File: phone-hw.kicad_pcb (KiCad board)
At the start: 2 copper layers, 66 x 100 mm, 73 parts, among them J1 USB_C_Receptacle_USB2.0, J2 Conn_01x06, J4 SIM_Card, J5 BATT+, J6 BATT-, Q1 BC847BLT3G, Q2 S9015, Q3 RU8205G, SW1 SW_Push, SW2 SW_Push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

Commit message: route pcb
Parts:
- added R20: 10k, Resistor_SMD:R_0603_1608Metric_Pad1.05x0.95mm_HandSolder, F.Cu at (41.8, 89.2)
- J2: value Conn_01x06 -> Micro_SD_Card; footprint Connector:Tag-Connect_TC2030-IDC-NL_2x03_P1.27mm_Vertical -> Connector_Card:microSD_HC_Hirose_DM3D-SF; moved to B.Cu
- moved J2 62.0 mm to (29.5, 99.0), turned to 180 degrees
- moved R6 28.8 mm to (31.2, 84.8), turned to 180 degrees
- moved C4 0.56 mm to (29.8, 56.0)
- moved R8 0.50 mm to (26.5, 86.8)
- moved C15 0.25 mm to (53.8, 108.0)
- moved R7 0.25 mm to (30.5, 86.8)
- moved C24 0.13 mm to (74.5, 91.9), turned to 0 degrees
- turned R18 to 270 degrees
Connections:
- net JTAG_MTDI renamed SD_~CS
- J2 pad 1: VDD -> Net-(J2-Pad1)
- J2 pad 3: JTAG_MTCK -> SD_MOSI
- J2 pad 4: JTAG_MTMS -> VDD
- J2 pad 5: JTAG_MTDO -> SD_CLK
- U1 pad 13: JTAG_MTMS -> SD_CLK
- U1 pad 16: JTAG_MTCK -> SD_MISO
- U1 pad 23: JTAG_MTDO -> SD_MOSI
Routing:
- net GND_OUT: track 0.00 -> 274.1 mm, vias 0 -> 28
- net +BATT: track 0.00 -> 256.0 mm, vias 0 -> 10
- net VDD: track 0.00 -> 254.5 mm, vias 0 -> 22
- net LCD_TE: track 0.00 -> 115.5 mm, vias 0 -> 4
- net Net-(R1-Pad2): track 0.00 -> 114.4 mm, vias 0 -> 6
- net LCD_DC: track 0.00 -> 111.0 mm, vias 0 -> 2
- net LCD_SCL: track 0.00 -> 109.2 mm, vias 0 -> 2
- net LCD_SDA: track 0.00 -> 108.7 mm, vias 0 -> 2
- net LCD_~CS: track 0.00 -> 104.0 mm
- net GPS_RXD: track 0.00 -> 91.4 mm, vias 0 -> 2
- net BATT_~STDBY: track 0.00 -> 90.6 mm, vias 0 -> 6
- net Net-(SW2-Pad1): track 0.00 -> 88.8 mm, vias 0 -> 6
- net GPS_RESET: track 0.00 -> 87.6 mm, vias 0 -> 2
- net BATT_~CHRG: track 0.00 -> 87.6 mm
- net GPS_TXD: track 0.00 -> 81.8 mm, vias 0 -> 2
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- added copper zone on B.Cu, net GND_OUT

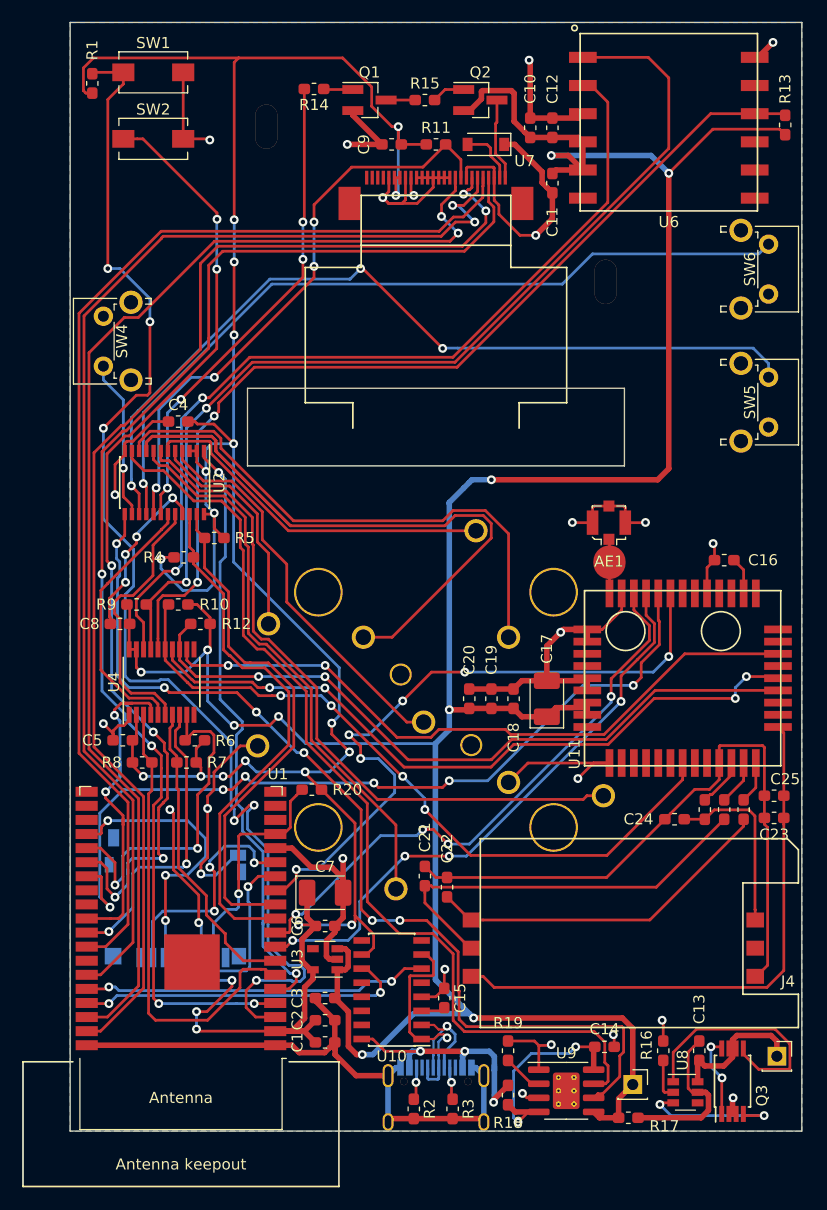
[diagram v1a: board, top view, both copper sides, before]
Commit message: add mounting holes
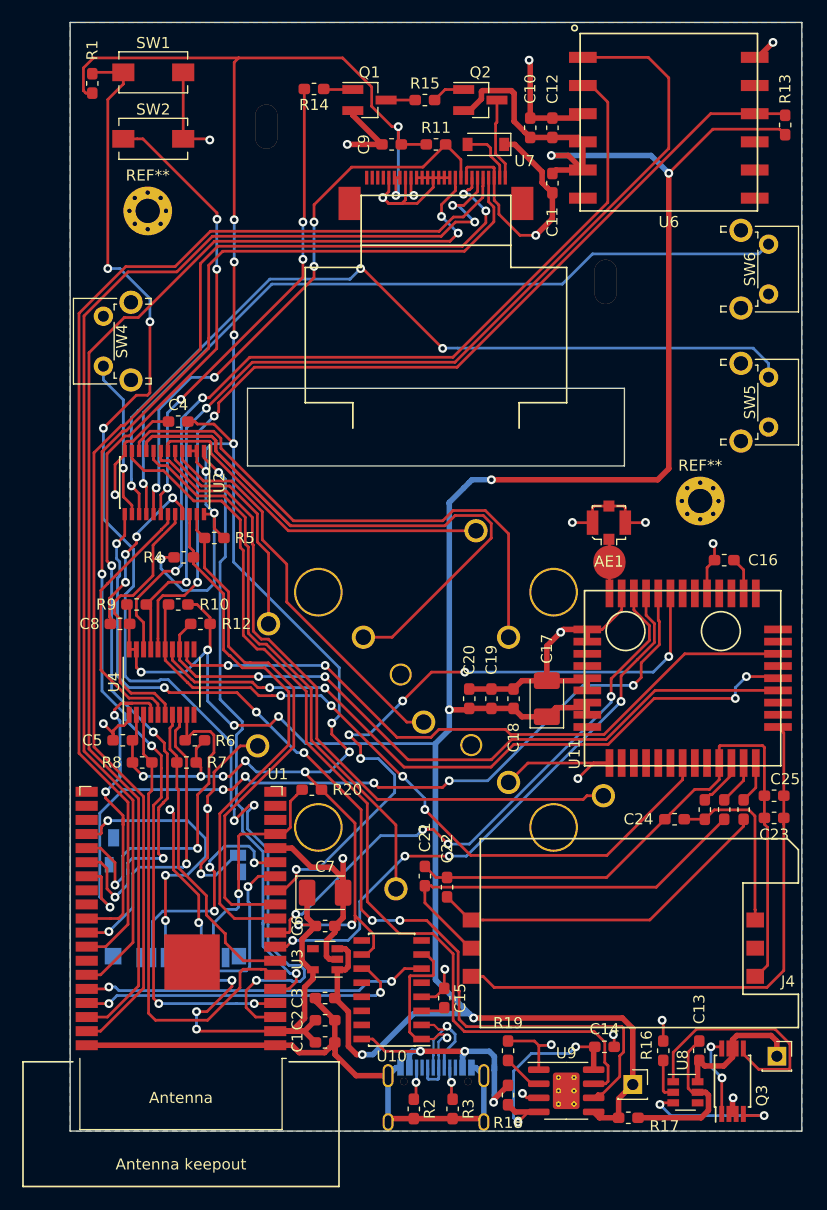
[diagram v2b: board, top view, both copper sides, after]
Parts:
- added REF**: MountingHole_2.2mm_M2_Pad_Via, MountingHole:MountingHole_2.2mm_M2_Pad_Via, F.Cu at (27.0, 37.0)
- added REF**: MountingHole_2.2mm_M2_Pad_Via, MountingHole:MountingHole_2.2mm_M2_Pad_Via, F.Cu at (76.8, 63.2)
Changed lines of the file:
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@@
     (thickness 1.6)
     (drawings 4)
-    (tracks 1560)
+    (tracks 1562)
     (zones 0)
-    (modules 74)
+    (modules 76)
     (nets 127)
   )
@@
   )
   (setup
-    (last_trace_width 0.5)
+    (last_trace_width 0.25)
     (user_trace_width 0.5)
     (user_trace_width 2.915)
@@
     (add_net VDD)
   )
+  (module MountingHole:MountingHole_2.2mm_M2_Pad_Via (layer F.Cu)
+    (at 27 37)
+    (descr "Mounting Hole 2.2mm, M2")
+    (tags "mounting hole 2.2mm m2")
+    (attr virtual)
+    (fp_text reference REF** (at 0 -3.2) (layer F.SilkS)
+      (effects (font (size 1 1) (thickness 0.15)))
+    )
+    (fp_text value MountingHole_2.2mm_M2_Pad_Via (at 0 3.2) (layer F.Fab)
+      (effects (font (size 1 1) (thickness 0.15)))
+    )
+    (fp_circle (center 0 0) (end 2.45 0) (layer F.CrtYd) (width 0.05))
+    (fp_circle (center 0 0) (end 2.2 0) (layer Cmts.User) (width 0.15))
+    (fp_text user %R (at 0.3 0) (layer F.Fab)
+      (effects (font (size 1 1) (thickness 0.15)))
+    )
+    (pad 1 thru_hole circle (at 1.166726 -1.166726) (size 0.7 0.7) (drill 0.4) (layers *.Cu *.Mask))
+    (pad 1 thru_hole circle (at 0 -1.65) (size 0.7 0.7) (drill 0.4) (layers *.Cu *.Mask))
+    (pad 1 thru_hole circle (at -1.166726 -1.166726) (size 0.7 0.7) (drill 0.4) (layers *.Cu *.Mask))
+    (pad 1 thru_hole circle (at -1.65 0) (size 0.7 0.7) (drill 0.4) (layers *.Cu *.Mask))
+    (pad 1 thru_hole circle (at -1.166726 1.166726) (size 0.7 0.7) (drill 0.4) (layers *.Cu *.Mask))
+    (pad 1 thru_hole circle (at 0 1.65) (size 0.7 0.7) (drill 0.4) (layers *.Cu *.Mask))
+    (pad 1 thru_hole circle (at 1.166726 1.166726) (size 0.7 0.7) (drill 0.4) (layers *.Cu *.Mask))
+    (pad 1 thru_hole circle (at 1.65 0) (size 0.7 0.7) (drill 0.4) (layers *.Cu *.Mask))
+    (pad 1 thru_hole circle (at 0 0) (size 4.4 4.4) (drill 2.2) (layers *.Cu *.Mask))
+  )
+  (module MountingHole:MountingHole_2.2mm_M2_Pad_Via (layer F.Cu)
+    (at 76.833274 63.166726)
+    (descr "Mounting Hole 2.2mm, M2")
+    (tags "mounting hole 2.2mm m2")
+    (attr virtual)
+    (fp_text reference REF** (at 0 -3.2) (layer F.SilkS)
+      (effects (font (size 1 1) (thickness 0.15)))
+    )
+    (fp_text value MountingHole_2.2mm_M2_Pad_Via (at 0 3.2) (layer F.Fab)
+      (effects (font (size 1 1) (thickness 0.15)))
+    )
+    (fp_circle (center 0 0) (end 2.45 0) (layer F.CrtYd) (width 0.05))
+    (fp_circle (center 0 0) (end 2.2 0) (layer Cmts.User) (width 0.15))
+    (fp_text user %R (at 0.3 0) (layer F.Fab)
+      (effects (font (size 1 1) (thickness 0.15)))
+    )
+    (pad 1 thru_hole circle (at 1.166726 -1.166726) (size 0.7 0.7) (drill 0.4) (layers *.Cu *.Mask))
+    (pad 1 thru_hole circle (at 0 -1.65) (size 0.7 0.7) (drill 0.4) (layers *.Cu *.Mask))
+    (pad 1 thru_hole circle (at -1.166726 -1.166726) (size 0.7 0.7) (drill 0.4) (layers *.Cu *.Mask))
+    (pad 1 thru_hole circle (at -1.65 0) (size 0.7 0.7) (drill 0.4) (layers *.Cu *.Mask))
+    (pad 1 thru_hole circle (at -1.166726 1.166726) (size 0.7 0.7) (drill 0.4) (layers *.Cu *.Mask))
+    (pad 1 thru_hole circle (at 0 1.65) (size 0.7 0.7) (drill 0.4) (layers *.Cu *.Mask))
+    (pad 1 thru_hole circle (at 1.166726 1.166726) (size 0.7 0.7) (drill 0.4) (layers *.Cu *.Mask))
+    (pad 1 thru_hole circle (at 1.65 0) (size 0.7 0.7) (drill 0.4) (layers *.Cu *.Mask))
+    (pad 1 thru_hole circle (at 0 0) (size 4.4 4.4) (drill 2.2) (layers *.Cu *.Mask))
+  )
   (module Connector_Coaxial:U.FL_Molex_MCRF_73412-0110_Vertical (layer F.Cu)
     (at 68.6 65.12)
@@
   (segment (start 30.5 95.9) (end 30.5 86.30449) (width 0.25) (layer F.Cu) (net 79))
   (via (at 30.5 95.9) (size 0.8) (drill 0.4) (layers F.Cu B.Cu) (net 79))
-  (segment (start 57.25 34.75) (end 57.25 34) (width 0.25) (layer F.Cu) (net 80))
-  (segment (start 57.225009 34.774991) (end 57.25 34.75) (width 0.25) (layer F.Cu) (net 80))
-  (segment (start 55.45001 37.54999) (end 57.225009 35.774991) (width 0.25) (layer F.Cu) (net 80))
-  (segment (start 54.57501 37.54999) (end 55.45001 37.54999) (width 0.25) (layer F.Cu) (net 80))
-  (segment (start 21.5 103.365) (end 23.208002 103.365) (width 0.25) (layer F.Cu) (net 80))
-  (segment (start 28.205109 38.836301) (end 53.288699 38.836301) (width 0.25) (layer F.Cu) (net 80))
-  (segment (start 20.80002 46.24139) (end 28.205109 38.836301) (width 0.25) (layer F.Cu) (net 80))
-  (segment (start 53.288699 38.836301) (end 54.57501 37.54999) (width 0.25) (layer F.Cu) (net 80))
-  (segment (start 25.225001 90.334131) (end 20.80002 85.90915) (width 0.25) (layer F.Cu) (net 80))
-  (segment (start 57.225009 35.774991) (end 57.225009 34.774991) (width 0.25) (layer F.Cu) (net 80))
-  (segment (start 23.208002 103.365) (end 25.225001 101.348001) (width 0.25) (layer F.Cu) (net 80))
-  (segment (start 20.80002 85.90915) (end 20.80002 46.24139) (width 0.25) (layer F.Cu) (net 80))
-  (segment (start 25.225001 101.348001) (end 25.225001 90.334131) (width 0.25) (layer F.Cu) (net 80))
+  (segment (start 23.208002 103.365) (end 21.5 103.365) (width 0.25) (layer F.Cu) (net 80))
+  (segment (start 25.225001 101.348001) (end 23.208002 103.365) (width 0.25) (layer F.Cu) (net 80))
+  (segment (start 25.225001 90.334131) (end 25.225001 101.348001) (width 0.25) (layer F.Cu) (net 80))
+  (segment (start 20.80002 85.90915) (end 25.225001 90.334131) (width 0.25) (layer F.Cu) (net 80))
+  (segment (start 57.225009 35.774991) (end 55.45001 37.54999) (width 0.25) (layer F.Cu) (net 80))
+  (segment (start 32.655883 38.836301) (end 29.471479 42.020705) (width 0.25) (layer F.Cu) (net 80))
+  (segment (start 53.288699 38.836301) (end 32.655883 38.836301) (width 0.25) (layer F.Cu) (net 80))
+  (segment (start 25.020705 42.020705) (end 20.80002 46.24139) (width 0.25) (layer F.Cu) (net 80))
+  (segment (start 54.57501 37.54999) (end 53.288699 38.836301) (width 0.25) (layer F.Cu) (net 80))
+  (segment (start 29.471479 42.020705) (end 25.020705 42.020705) (width 0.25) (layer F.Cu) (net 80))
+  (segment (start 55.45001 37.54999) (end 54.57501 37.54999) (width 0.25) (layer F.Cu) (net 80))
+  (segment (start 20.80002 46.24139) (end 20.80002 85.90915) (width 0.25) (layer F.Cu) (net 80))
+  (segment (start 57.225009 34.774991) (end 57.225009 35.774991) (width 0.25) (layer F.Cu) (net 80))
+  (segment (start 57.25 34.75) (end 57.225009 34.774991) (width 0.25) (layer F.Cu) (net 80))
+  (segment (start 57.25 34) (end 57.25 34.75) (width 0.25) (layer F.Cu) (net 80))
   (via (at 56.5 38) (size 0.8) (drill 0.4) (layers F.Cu B.Cu) (net 82))
   (via (at 54.5 36.5) (size 0.8) (drill 0.4) (layers F.Cu B.Cu) (net 82))
@@
   (segment (start 55.5 36.5) (end 54.5 36.5) (width 0.25) (layer F.Cu) (net 82))
   (segment (start 56.75 35.25) (end 55.5 36.5) (width 0.25) (layer F.Cu) (net 82))
-  (segment (start 28.391509 39.286311) (end 53.475099 39.286311) (width 0.25) (layer F.Cu) (net 82))
-  (segment (start 28.223998 39.5) (end 28.223998 39.453822) (width 0.25) (layer F.Cu) (net 82))
-  (segment (start 54.76141 38) (end 56.5 38) (width 0.25) (layer F.Cu) (net 82))
-  (segment (start 21.25003 85.72275) (end 21.25003 46.473968) (width 0.25) (layer F.Cu) (net 82))
-  (segment (start 25.67501 90.14773) (end 21.25003 85.72275) (width 0.25) (layer F.Cu) (net 82))
-  (segment (start 53.475099 39.286311) (end 54.76141 38) (width 0.25) (layer F.Cu) (net 82))
-  (segment (start 25.675011 102.979989) (end 25.67501 90.14773) (width 0.25) (layer F.Cu) (net 82))
-  (segment (start 22.75 105.905) (end 25.675011 102.979989) (width 0.25) (layer F.Cu) (net 82))
-  (segment (start 28.223998 39.453822) (end 28.391509 39.286311) (width 0.25) (layer F.Cu) (net 82))
-  (segment (start 21.25003 46.473968) (end 28.223998 39.5) (width 0.25) (layer F.Cu) (net 82))
-  (segment (start 21.5 105.905) (end 22.75 105.905) (width 0.25) (layer F.Cu) (net 82))
+  (segment (start 25.675011 102.979989) (end 22.75 105.905) (width 0.25) (layer F.Cu) (net 82))
+  (segment (start 25.67501 90.14773) (end 25.675011 102.979989) (width 0.25) (layer F.Cu) (net 82))
+  (segment (start 21.25003 46.473968) (end 21.25003 85.72275) (width 0.25) (layer F.Cu) (net 82))
+  (segment (start 25.223998 42.5) (end 21.25003 46.473968) (width 0.25) (layer F.Cu) (net 82))
+  (segment (start 29.628592 42.5) (end 25.223998 42.5) (width 0.25) (layer F.Cu) (net 82))
+  (segment (start 22.75 105.905) (end 21.5 105.905) (width 0.25) (layer F.Cu) (net 82))
+  (segment (start 53.475099 39.286311) (end 32.84228 39.286312) (width 0.25) (layer F.Cu) (net 82))
+  (segment (start 32.84228 39.286312) (end 29.628592 42.5) (width 0.25) (layer F.Cu) (net 82))
+  (segment (start 21.25003 85.72275) (end 25.67501 90.14773) (width 0.25) (layer F.Cu) (net 82))
+  (segment (start 54.76141 38) (end 53.475099 39.286311) (width 0.25) (layer F.Cu) (net 82))
+  (segment (start 56.5 38) (end 54.76141 38) (width 0.25) (layer F.Cu) (net 82))
   (via (at 23.5 107) (size 0.8) (drill 0.4) (layers F.Cu B.Cu) (net 83))
   (segment (start 23.325 107.175) (end 23.5 107) (width 0.25) (layer F.Cu) (net 83))

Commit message: move mounting holes
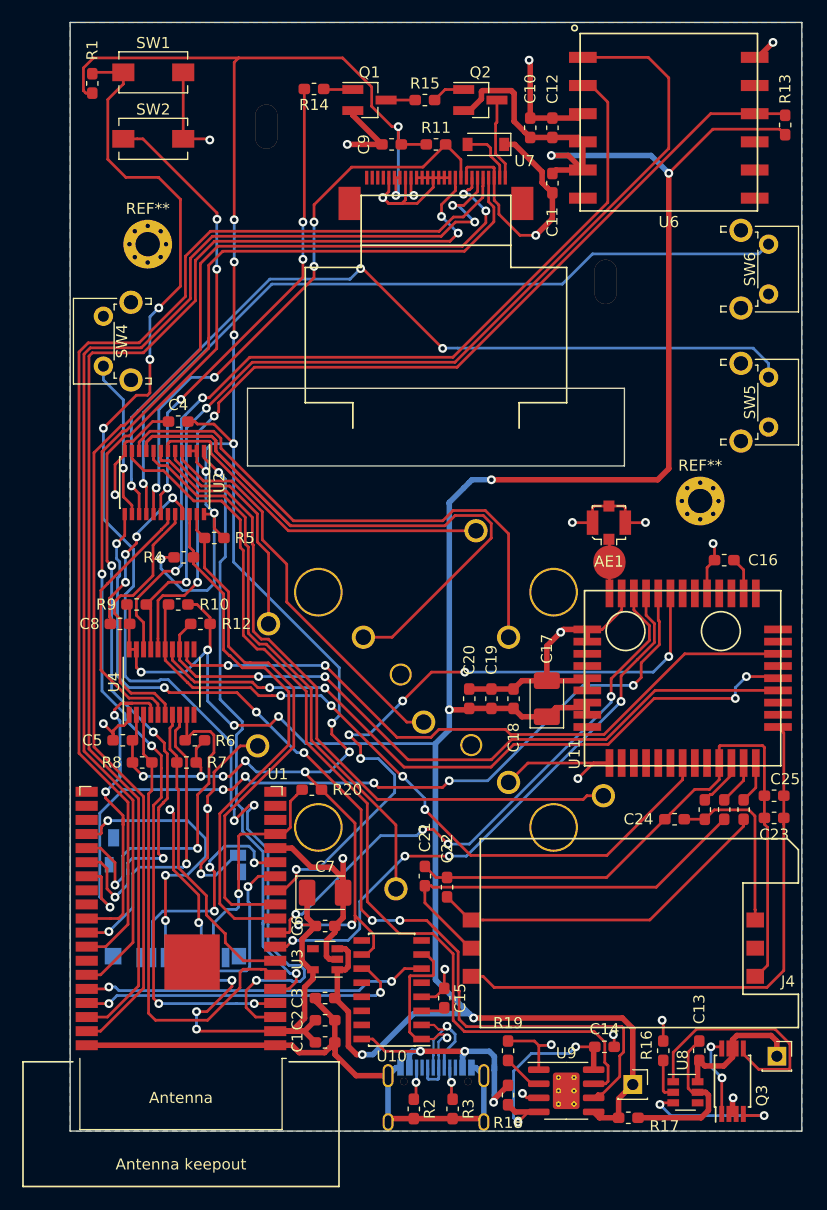
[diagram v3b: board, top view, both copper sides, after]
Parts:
- moved REF** 3.00 mm to (27.0, 40.0)
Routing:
- net Net-(R1-Pad2): track 114.4 -> 117.8 mm
- net LCD_SDA: track 108.7 -> 110.7 mm

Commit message: add silkscreen info and battery indicators
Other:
- board text added: "+BATT"
- board text added: "-BATT"
- board text added: "phone-hw rev A - 2019-05-15"
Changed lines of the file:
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@@
   (general
     (thickness 1.6)
-    (drawings 4)
+    (drawings 11)
     (tracks 1572)
     (zones 0)
@@
     )
   )
+  (gr_text +BATT (at 70.75 114.5 270) (layer B.SilkS)
+    (effects (font (size 1 1) (thickness 0.15)) (justify left mirror))
+  )
+  (gr_text -BATT (at 83.75 111.75 270) (layer B.SilkS)
+    (effects (font (size 1 1) (thickness 0.15)) (justify left mirror))
+  )
+  (gr_line (start 65 101) (end 82 101) (layer B.SilkS) (width 0.12))
+  (gr_line (start 65 105) (end 65 101) (layer B.SilkS) (width 0.12))
+  (gr_line (start 82 105) (end 65 105) (layer B.SilkS) (width 0.12))
+  (gr_line (start 82 101) (end 82 105) (layer B.SilkS) (width 0.12))
+  (gr_text "phone-hw\nrev A - 2019-05-15" (at 82 103) (layer B.SilkS)
+    (effects (font (size 1 1) (thickness 0.15)) (justify left mirror))
+  )
   (gr_line (start 86 120) (end 20 120) (layer Edge.Cuts) (width 0.05))
